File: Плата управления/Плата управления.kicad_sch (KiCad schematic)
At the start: 0 parts

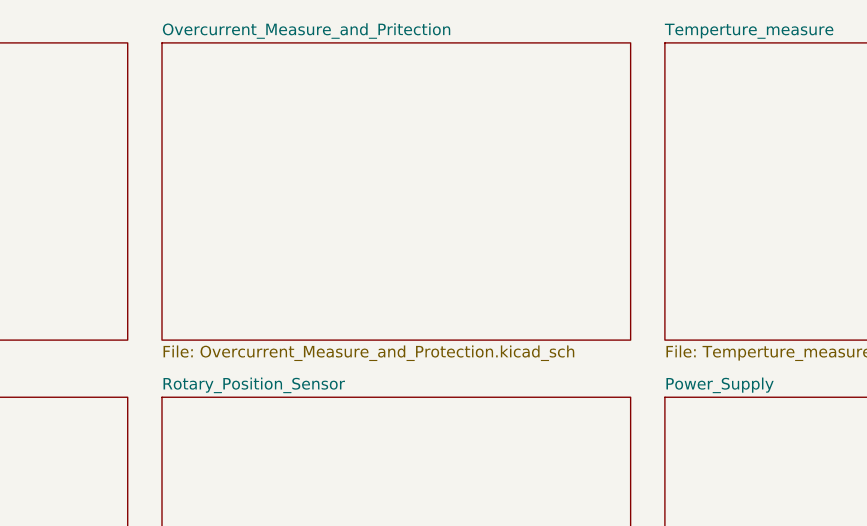
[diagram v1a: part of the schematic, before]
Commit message: Добавил питание MCU и кварц на 8Мгц
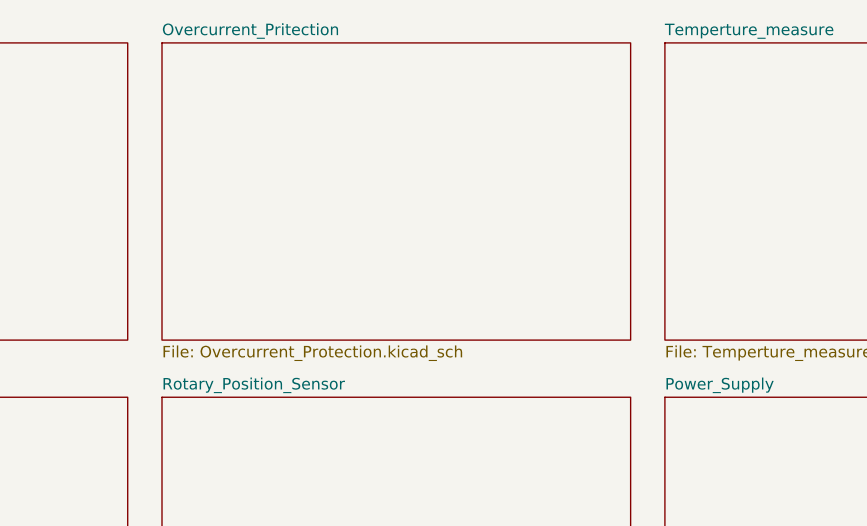
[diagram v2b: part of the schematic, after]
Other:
- sheet Overcurrent_Measure_and_Pritection renamed Overcurrent_Pritection
- sheet Overcurrent_Pritection: file Overcurrent_Measure_and_Protection.kicad_sch -> Overcurrent_Protection.kicad_sch
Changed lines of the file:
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@@
   (sheet (at 128.27 55.88) (size 52.07 33.02) (fields_autoplaced)
     (stroke (width 0.1524) (type solid))
-    (fill (color 0 0 0 0.0000))
+    (fill (color 0 194 0 1.0000))
     (property "Sheetname" "Power_Supply" (at 128.27 55.1684 0)
       (effects (font (size 1.27 1.27)) (justify left bottom))
@@
     (stroke (width 0.1524) (type solid))
     (fill (color 0 194 0 1.0000))
-    (property "Sheetname" "Overcurrent_Measure_and_Pritection" (at 72.39 15.7984 0)
+    (property "Sheetname" "Overcurrent_Pritection" (at 72.39 15.7984 0)
       (effects (font (size 1.27 1.27)) (justify left bottom))
     )
-    (property "Sheetfile" "Overcurrent_Measure_and_Protection.kicad_sch" (at 72.39 50.1146 0)
+    (property "Sheetfile" "Overcurrent_Protection.kicad_sch" (at 72.39 50.1146 0)
       (effects (font (size 1.27 1.27)) (justify left top))
     )
+    (property "Поле2" "" (at 72.39 16.51 0)
+      (effects (font (size 1.27 1.27)) hide)
+    )
     (instances

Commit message: Привел в порядок схему
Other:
- note added: "CAN"
- note added: "Connectors"
- note added: "Driver"
- note added: "MCU"
- note added: "Overcurrent Protection"
- note added: "Power Supply"
- note added: "Rotary Position Sensor"
- note added: "Temperture Measure"
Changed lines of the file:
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@@
 (kicad_sch (version 20230121) (generator eeschema)
   (paper "A4")
+  (text "Overcurrent \nProtection" (at 85.09 35.56 0)
+    (effects (font (size 3 3) (thickness 0.6) bold) (justify left bottom))
+  )
+  (text "Power\nSupply\n" (at 146.05 74.93 0)
+    (effects (font (size 3 3) (thickness 0.6) bold) (justify left bottom))
+  )
+  (text "Temperture\nMeasure" (at 142.24 35.56 0)
+    (effects (font (size 3 3) (thickness 0.6) bold) (justify left bottom))
+  )
+  (text "CAN" (at 205.74 73.66 0)
+    (effects (font (size 3 3) (thickness 0.6) bold) (justify left bottom))
+  )
+  (text "Connectors" (at 198.12 33.02 0)
+    (effects (font (size 3 3) (thickness 0.6) bold) (justify left bottom))
+  )
+  (text "Driver" (at 35.56 33.02 0)
+    (effects (font (size 3 3) (thickness 0.6) bold) (justify left bottom))
+  )
+  (text "MCU" (at 38.1 73.66 0)
+    (effects (font (size 3 3) (thickness 0.6) bold) (justify left bottom))
+  )
+  (text "Rotary\nPosition\nSensor\n" (at 90.17 78.74 0)
+    (effects (font (size 3 3) (thickness 0.6) bold) (justify left bottom))
+  )
   (sheet (at 16.51 16.51) (size 52.07 33.02) (fields_autoplaced)
     (stroke (width 0.1524) (type solid))
-    (fill (color 0 194 0 1.0000))
+    (fill (color 0 0 0 0.0000))
     (property "Sheetname" "Driver" (at 16.51 15.7984 0)
-      (effects (font (size 1.27 1.27)) (justify left bottom))
+      (effects (font (size 1.27 1.27) bold) (justify left bottom))
     )
     (property "Sheetfile" "Driver.kicad_sch" (at 16.51 50.1146 0)
@@
   (sheet (at 16.51 55.88) (size 52.07 33.02) (fields_autoplaced)
     (stroke (width 0.1524) (type solid))
-    (fill (color 194 0 0 1.0000))
+    (fill (color 0 0 0 0.0000))
     (property "Sheetname" "MCU" (at 16.51 55.1684 0)
       (effects (font (size 1.27 1.27)) (justify left bottom))
@@
   (sheet (at 128.27 55.88) (size 52.07 33.02) (fields_autoplaced)
     (stroke (width 0.1524) (type solid))
-    (fill (color 0 194 0 1.0000))
+    (fill (color 0 0 0 0.0000))
     (property "Sheetname" "Power_Supply" (at 128.27 55.1684 0)
       (effects (font (size 1.27 1.27)) (justify left bottom))
@@
   (sheet (at 184.15 55.88) (size 52.07 33.02) (fields_autoplaced)
     (stroke (width 0.1524) (type solid))
-    (fill (color 0 194 0 1.0000))
+    (fill (color 0 0 0 0.0000))
     (property "Sheetname" "CAN" (at 184.15 55.1684 0)
       (effects (font (size 1.27 1.27)) (justify left bottom))
@@
   (sheet (at 72.39 55.88) (size 52.07 33.02) (fields_autoplaced)
     (stroke (width 0.1524) (type solid))
-    (fill (color 0 194 0 1.0000))
+    (fill (color 0 0 0 0.0000))
     (property "Sheetname" "Rotary_Position_Sensor" (at 72.39 55.1684 0)
       (effects (font (size 1.27 1.27)) (justify left bottom))
@@
   (sheet (at 72.39 16.51) (size 52.07 33.02) (fields_autoplaced)
     (stroke (width 0.1524) (type solid))
-    (fill (color 0 194 0 1.0000))
+    (fill (color 0 0 0 0.0000))
     (property "Sheetname" "Overcurrent_Pritection" (at 72.39 15.7984 0)
-      (effects (font (size 1.27 1.27)) (justify left bottom))
+      (effects (font (size 1.27 1.27) bold) (justify left bottom))
     )
     (property "Sheetfile" "Overcurrent_Protection.kicad_sch" (at 72.39 50.1146 0)
@@
   (sheet (at 128.27 16.51) (size 52.07 33.02) (fields_autoplaced)
     (stroke (width 0.1524) (type solid))
-    (fill (color 0 194 0 1.0000))
+    (fill (color 0 0 0 0.0000))
     (property "Sheetname" "Temperture_measure" (at 128.27 15.7984 0)
       (effects (font (size 1.27 1.27)) (justify left bottom))

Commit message: Добавил EEPROM
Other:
- removed sheet Rotary_Position_Sensor
- added sheet EEPROM (EEPROM.kicad_sch)
- added sheet RS485 (RS485.kicad_sch)
- added sheet RS486 (RS485.kicad_sch)
- note added: "EEPROM"
- note added: "RS485"
- note removed: "Rotary Position Sensor"
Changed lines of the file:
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@@
+    (effects (font (size 3 3) (thickness 0.6) bold) (justify left bottom))
+  )
+  (text "RS485" (at 35.56 113.03 0)
     (effects (font (size 3 3) (thickness 0.6) bold) (justify left bottom))
   )
@@
     (effects (font (size 3 3) (thickness 0.6) bold) (justify left bottom))
   )
-  (text "Rotary\nPosition\nSensor\n" (at 90.17 78.74 0)
+  (text "EEPROM" (at 91.44 73.66 0)
     (effects (font (size 3 3) (thickness 0.6) bold) (justify left bottom))
   )
@@
       (project "Плата управления"
         (path "/75f4c67c-bbde-4446-8f82-67797a1b269f" (page "2"))
+      )
+    )
+  )
+  (sheet (at 72.39 95.25) (size 52.07 33.02) (fields_autoplaced)
+    (stroke (width 0.1524) (type solid))
+    (fill (color 0 0 0 0.0000))
+    (property "Sheetname" "RS486" (at 72.39 94.5384 0)
+      (effects (font (size 1.27 1.27)) (justify left bottom))
+    )
+    (property "Sheetfile" "RS485.kicad_sch" (at 72.39 128.8546 0)
+      (effects (font (size 1.27 1.27)) (justify left top))
+    )
+    (property "Поле2" "" (at 72.39 95.25 0)
+      (effects (font (size 1.27 1.27)) hide)
+    )
+    (instances
+      (project "Плата управления"
+        (path "/75f4c67c-bbde-4446-8f82-67797a1b269f" (page "11"))
       )
     )
@@
     (stroke (width 0.1524) (type solid))
     (fill (color 0 0 0 0.0000))
-    (property "Sheetname" "Rotary_Position_Sensor" (at 72.39 55.1684 0)
+    (property "Sheetname" "EEPROM" (at 72.39 55.1684 0)
       (effects (font (size 1.27 1.27)) (justify left bottom))
     )
-    (property "Sheetfile" "Rotary_Position_Sensor.kicad_sch" (at 72.39 89.4846 0)
+    (property "Sheetfile" "EEPROM.kicad_sch" (at 72.39 89.4846 0)
       (effects (font (size 1.27 1.27)) (justify left top))
     )
+    (property "Поле2" "" (at 72.39 55.88 0)
+      (effects (font (size 1.27 1.27)) hide)
+    )
     (instances
+      (project "Плата управления"
+        (path "/75f4c67c-bbde-4446-8f82-67797a1b269f" (page "10"))
+      )
+    )
+  )
+  (sheet (at 16.51 95.25) (size 52.07 33.02) (fields_autoplaced)
+    (stroke (width 0.1524) (type solid))
+    (fill (color 0 0 0 0.0000))
+    (property "Sheetname" "RS485" (at 16.51 94.5384 0)
+      (effects (font (size 1.27 1.27)) (justify left bottom))
+    )
+    (property "Sheetfile" "RS485.kicad_sch" (at 16.51 128.8546 0)
+      (effects (font (size 1.27 1.27)) (justify left top))
+    )
+    (property "Поле2" "" (at 16.51 95.25 0)
+      (effects (font (size 1.27 1.27)) hide)
+    )
+    (instances

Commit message: Расставил компоненты по плате
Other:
- sheet RS486 renamed JTAG
- sheet JTAG: file RS485.kicad_sch -> JTAG.kicad_sch
- note added: "JTAG"
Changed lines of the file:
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@@
+    (effects (font (size 3 3) (thickness 0.6) bold) (justify left bottom))
+  )
+  (text "JTAG" (at 93.98 113.03 0)
     (effects (font (size 3 3) (thickness 0.6) bold) (justify left bottom))
   )
@@
     (stroke (width 0.1524) (type solid))
     (fill (color 0 0 0 0.0000))
-    (property "Sheetname" "RS486" (at 72.39 94.5384 0)
+    (property "Sheetname" "JTAG" (at 72.39 94.5384 0)
       (effects (font (size 1.27 1.27)) (justify left bottom))
     )
-    (property "Sheetfile" "RS485.kicad_sch" (at 72.39 128.8546 0)
+    (property "Sheetfile" "JTAG.kicad_sch" (at 72.39 128.8546 0)
       (effects (font (size 1.27 1.27)) (justify left top))
     )

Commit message: Собираю документацию
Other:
- sheet JTAG renamed SWD
- sheet SWD: file JTAG.kicad_sch -> SWD.kicad_sch
- note added: "SWD"
- note removed: "JTAG"
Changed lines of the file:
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@@
     (effects (font (size 3 3) (thickness 0.6) bold) (justify left bottom))
   )
-  (text "JTAG" (at 93.98 113.03 0)
+  (text "SWD" (at 93.98 113.03 0)
     (effects (font (size 3 3) (thickness 0.6) bold) (justify left bottom))
   )
@@
     (stroke (width 0.1524) (type solid))
     (fill (color 0 0 0 0.0000))
-    (property "Sheetname" "JTAG" (at 72.39 94.5384 0)
+    (property "Sheetname" "SWD" (at 72.39 94.5384 0)
       (effects (font (size 1.27 1.27)) (justify left bottom))
     )
-    (property "Sheetfile" "JTAG.kicad_sch" (at 72.39 128.8546 0)
+    (property "Sheetfile" "SWD.kicad_sch" (at 72.39 128.8546 0)
       (effects (font (size 1.27 1.27)) (justify left top))
     )

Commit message: Добавил документы
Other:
- note added: "FRAM"
- note added: "Драйвера"
- note added: "Защита по току ЗПТ"
- note added: "Питание"
- note added: "Разъёмы"
- note added: "Температура силовой платы"
- note removed: "Connectors"
- note removed: "Driver"
- note removed: "EEPROM"
- note removed: "Overcurrent Protection"
- note removed: "Power Supply"
- note removed: "Temperture Measure"
- title: (none) -> Плата управления ЭЛП схема электрическая принципиальная

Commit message: Версия под отчёт
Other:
- added sheet Connection_list (Connection_list.kicad_sch)
- note added: "Схема электрическая"
- note added: "принципиальная"
- note removed: "CAN"
- note removed: "FRAM"
- note removed: "MCU"
- note removed: "RS485"
- note removed: "SWD"
- note removed: "Драйвера"
- note removed: "Защита по току ЗПТ"
- note removed: "Питание"
- note removed: "Разъёмы"
- note removed: "Температура силовой платы"
- company: (none) -> Московский Политех
- title: Плата управления ЭЛП схема электрическая принципиальная -> Узел управления
